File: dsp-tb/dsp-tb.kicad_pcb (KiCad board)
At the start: 2 copper layers, 24 parts, among them J10 USB_C_Receptacle_USB2.0, J2 Conn_ARM_SWD_TagConnect_TC2030, J9 104031-0811, U1 STM32H723ZGTx, U10 FSUSB42UMX, U11 CS4270-CZZ, U12 TLV9301xDBV, U13 TLV9301xDBV, U14 TLV9301xDBV, U15 TLV9301xDBV, U2 TLV76733QWDRBxQ1, U4 NCP718xSN500, U5 D3V3XA4B10LP, U6 IS42S16800F-7BL-TR, U7 IS25LP080D-JNLE, U8 USB3318C-CP-TR, U9 ASDMB-xxxMHz

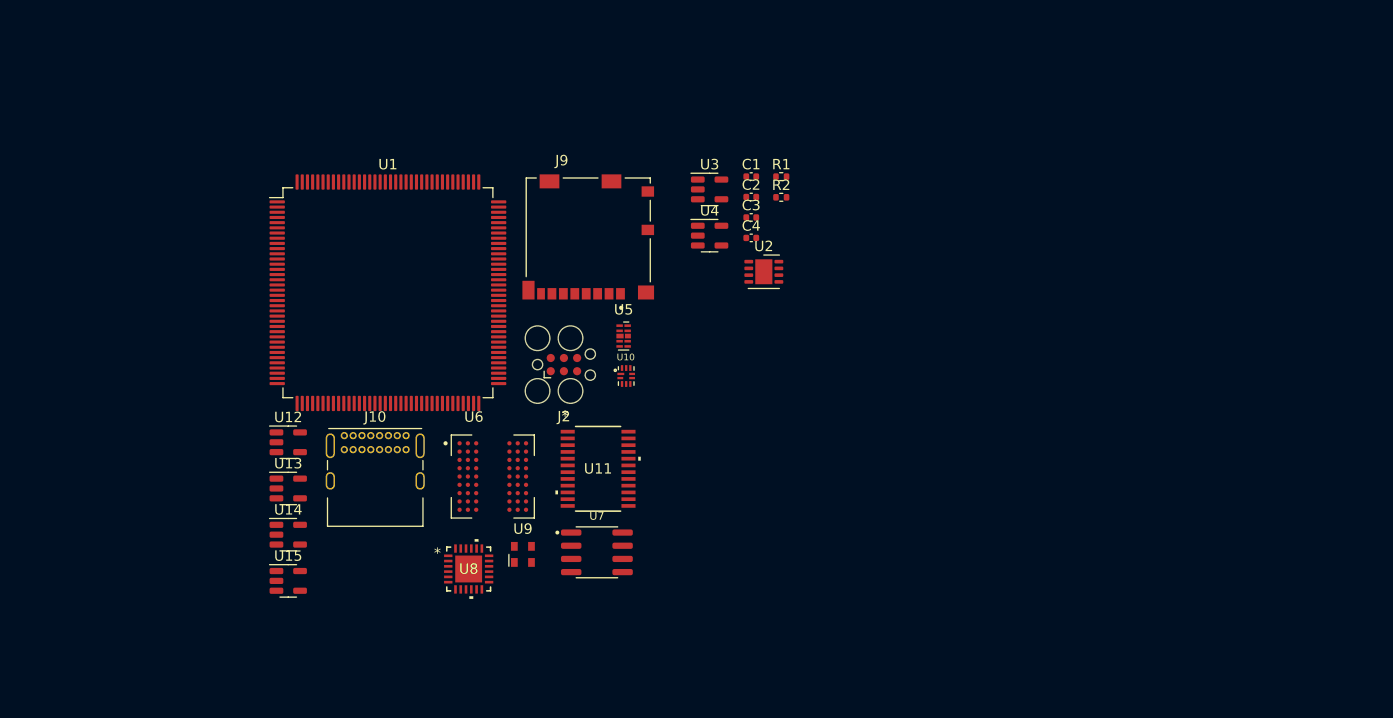
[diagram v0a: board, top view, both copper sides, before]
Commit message: dsp-tb: start to include external components for mcu
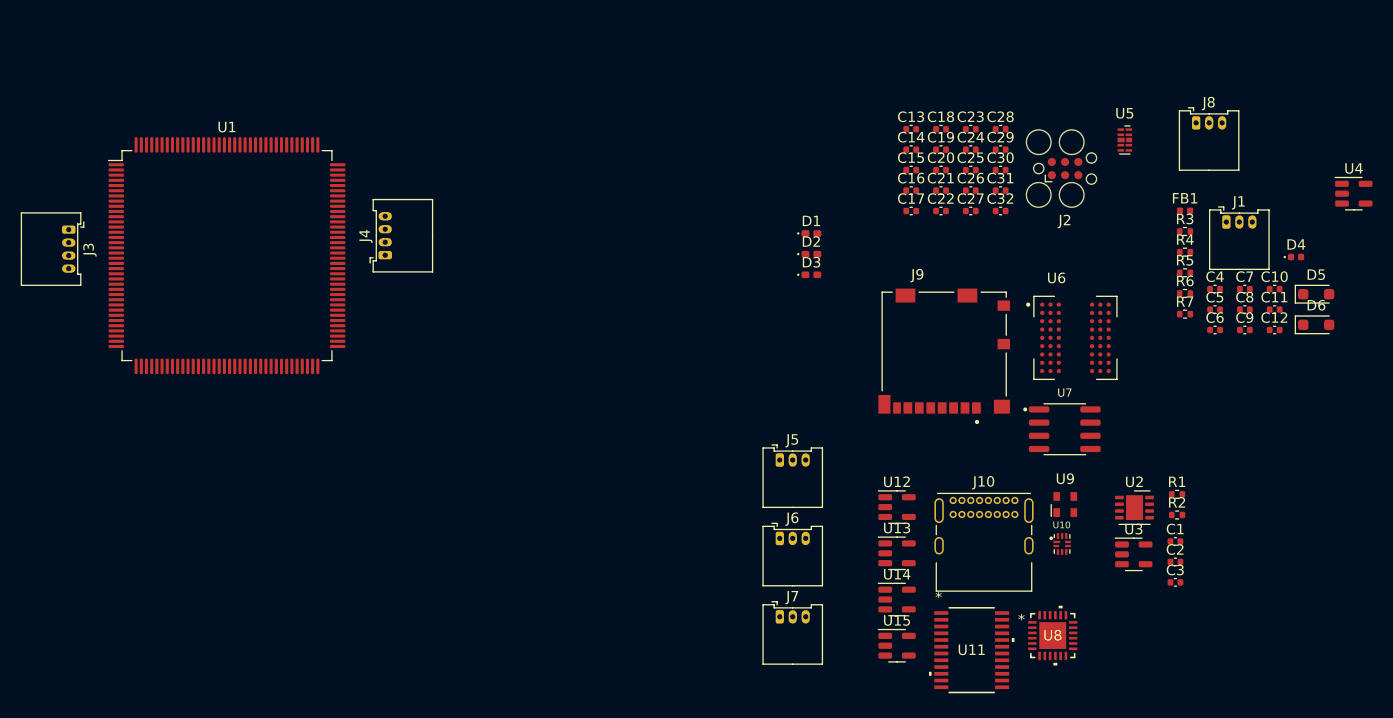
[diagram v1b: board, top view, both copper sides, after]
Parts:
- added C10: 47u, Capacitor_SMD:C_0402_1005Metric, F.Cu at (233.0, 87.0)
- added C11: 47u, Capacitor_SMD:C_0402_1005Metric, F.Cu at (233.0, 89.0)
- added C12: 47u, Capacitor_SMD:C_0402_1005Metric, F.Cu at (233.0, 91.0)
- added C13: 2u2, Capacitor_SMD:C_0402_1005Metric, F.Cu at (198.0, 71.6)
- added C14: 2u2, Capacitor_SMD:C_0402_1005Metric, F.Cu at (198.0, 73.6)
- added C15: 100n, Capacitor_SMD:C_0402_1005Metric, F.Cu at (198.0, 75.6)
- added C16: 100n, Capacitor_SMD:C_0402_1005Metric, F.Cu at (198.0, 77.6)
- added C17: 100n, Capacitor_SMD:C_0402_1005Metric, F.Cu at (198.0, 79.5)
- added C18: 100n, Capacitor_SMD:C_0402_1005Metric, F.Cu at (200.8, 71.6)
- added C19: 100n, Capacitor_SMD:C_0402_1005Metric, F.Cu at (200.8, 73.6)
- added C20: 100n, Capacitor_SMD:C_0402_1005Metric, F.Cu at (200.8, 75.6)
- added C21: 100n, Capacitor_SMD:C_0402_1005Metric, F.Cu at (200.8, 77.6)
- added C22: 100n, Capacitor_SMD:C_0402_1005Metric, F.Cu at (200.8, 79.5)
- added C23: 100n, Capacitor_SMD:C_0402_1005Metric, F.Cu at (203.7, 71.6)
- added C24: 100n, Capacitor_SMD:C_0402_1005Metric, F.Cu at (203.7, 73.6)
- added C25: 100n, Capacitor_SMD:C_0402_1005Metric, F.Cu at (203.7, 75.6)
- added C26: 100n, Capacitor_SMD:C_0402_1005Metric, F.Cu at (203.7, 77.6)
- added C27: 100n, Capacitor_SMD:C_0402_1005Metric, F.Cu at (203.7, 79.5)
- added C28: 100n, Capacitor_SMD:C_0402_1005Metric, F.Cu at (206.6, 71.6)
- added C29: 100n, Capacitor_SMD:C_0402_1005Metric, F.Cu at (206.6, 73.6)
- added C30: 100n, Capacitor_SMD:C_0402_1005Metric, F.Cu at (206.6, 75.6)
- added C31: 100n, Capacitor_SMD:C_0402_1005Metric, F.Cu at (206.6, 77.6)
- added C32: 2u2, Capacitor_SMD:C_0402_1005Metric, F.Cu at (206.6, 79.5)
- added C5: 2u2, Capacitor_SMD:C_0402_1005Metric, F.Cu at (227.2, 89.0)
- added C6: 2u2, Capacitor_SMD:C_0402_1005Metric, F.Cu at (227.2, 91.0)
- added C7: 2u2, Capacitor_SMD:C_0402_1005Metric, F.Cu at (230.1, 87.0)
- added C8: 2u2, Capacitor_SMD:C_0402_1005Metric, F.Cu at (230.1, 89.0)
- added C9: 47u, Capacitor_SMD:C_0402_1005Metric, F.Cu at (230.1, 91.0)
- added D1: RED, LED_SMD:LED_0402_1005Metric_Pad0.77x0.64mm_HandSolder, F.Cu at (188.4, 81.7)
- added D2: YLW, LED_SMD:LED_0402_1005Metric_Pad0.77x0.64mm_HandSolder, F.Cu at (188.4, 83.7)
- added D3: BLU, LED_SMD:LED_0402_1005Metric_Pad0.77x0.64mm_HandSolder, F.Cu at (188.4, 85.7)
- added D4: CG0402MLU-12G, Diode_SMD:D_0402_1005Metric, F.Cu at (235.0, 84.0)
- added D5: BAT165A, Diode_SMD:D_SOD-323_HandSoldering, F.Cu at (237.0, 87.5)
- added D6: BAT165A, Diode_SMD:D_SOD-323_HandSoldering, F.Cu at (237.0, 90.5)
- added FB1: FerriteBead, Inductor_SMD:L_0402_1005Metric, F.Cu at (224.3, 79.5)
- added J1: Conn_01x03, Connector_Molex:Molex_PicoBlade_53048-0310_1x03_P1.25mm_Horizontal, F.Cu at (228.3, 80.6)
- added J3: Conn_01x04, Connector_Molex:Molex_PicoBlade_53048-0410_1x04_P1.25mm_Horizontal, F.Cu at (116.8, 81.3)
- added J4: Conn_01x04, Connector_Molex:Molex_PicoBlade_53048-0410_1x04_P1.25mm_Horizontal, F.Cu at (147.3, 83.8)
- added J5: Conn_01x03, Connector_Molex:Molex_PicoBlade_53048-0310_1x03_P1.25mm_Horizontal, F.Cu at (185.3, 103.5)
- added J6: Conn_01x03, Connector_Molex:Molex_PicoBlade_53048-0310_1x03_P1.25mm_Horizontal, F.Cu at (185.3, 111.1)
- added J7: Conn_01x03, Connector_Molex:Molex_PicoBlade_53048-0310_1x03_P1.25mm_Horizontal, F.Cu at (185.3, 118.6)
- added J8: Conn_01x03, Connector_Molex:Molex_PicoBlade_53048-0310_1x03_P1.25mm_Horizontal, F.Cu at (225.4, 71.0)
- added R3: 47k, Resistor_SMD:R_0402_1005Metric, F.Cu at (224.3, 81.5)
- added R4: 15k, Resistor_SMD:R_0402_1005Metric, F.Cu at (224.3, 83.5)
- added R5: 47k, Resistor_SMD:R_0402_1005Metric, F.Cu at (224.3, 85.5)
- added R6: 91k, Resistor_SMD:R_0402_1005Metric, F.Cu at (224.3, 87.5)
- added R7: 10, Resistor_SMD:R_0402_1005Metric, F.Cu at (224.3, 89.5)
- U3: value ~ -> NCP718BSNADJT1G
- U4: value NCP718xSN500 -> NCP718BSNADJT1G
- moved U4 62.2 mm to (240.6, 77.9)
- moved U12 59.0 mm to (196.6, 108.0)
- moved U14 59.0 mm to (196.6, 116.9)
- moved U15 59.0 mm to (196.6, 121.4)
- moved U13 59.0 mm to (196.6, 112.5)
- moved J10 59.0 mm to (202.0, 107.4)
- moved U6 57.7 mm to (213.8, 91.7)
- moved U8 56.6 mm to (211.6, 120.4)
- moved C3 53.9 mm to (223.4, 115.3)
- moved U3 53.9 mm to (219.4, 112.6)
- moved C1 53.9 mm to (223.4, 111.3)
- moved C2 53.9 mm to (223.4, 113.3)
- moved U9 52.5 mm to (212.8, 107.8)
- moved J2 51.8 mm to (212.8, 75.4)
- moved U5 51.8 mm to (218.5, 72.7)
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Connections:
- C1 pad 1: Net-(U2-EN) -> Net-(D6-K)
- C2 pad 1: unconnected-(C2-Pad1) -> +3V3
- C2 pad 2: unconnected-(C2-Pad2) -> GND
- C3 pad 1: Net-(U2-OUT) -> Net-(D6-K)
- C4 pad 1: Net-(U3-EN) -> +5V
- C4 pad 2: unconnected-(C4-Pad2) -> GND
- R1 pad 1: Net-(U2-OUT) -> +3V3
- U1 pad 106: unconnected-(U1-VCAP-Pad106) -> Net-(C14-Pad1)
- U1 pad 71: unconnected-(U1-VCAP-Pad71) -> Net-(C13-Pad1)
- U2 pad 1: Net-(U2-OUT) -> +3V3
- U2 pad 5: Net-(U2-EN) -> Net-(D6-K)
- U2 pad 8: Net-(U2-EN) -> Net-(D6-K)
- U3 pad 1: Net-(U3-EN) -> Net-(D6-K)
- U3 pad 2: unconnected-(U3-GND-Pad2) -> GND
- U3 pad 3: Net-(U3-EN) -> Net-(D6-K)
- U3 pad 4: unconnected-(U3-ADJ-Pad4) -> Net-(U3-ADJ)
- U3 pad 5: unconnected-(U3-OUT-Pad5) -> +5V
- U4 pad 1: unconnected-(U4-IN-Pad1) -> +3V3
- U4 pad 2: unconnected-(U4-GND-Pad2) -> GND
- U4 pad 3: unconnected-(U4-EN-Pad3) -> +3V3
- U4 pad 4: unconnected-(U4-NC-Pad4) -> Net-(U4-ADJ)
- U4 pad 5: unconnected-(U4-OUT-Pad5) -> +1V8

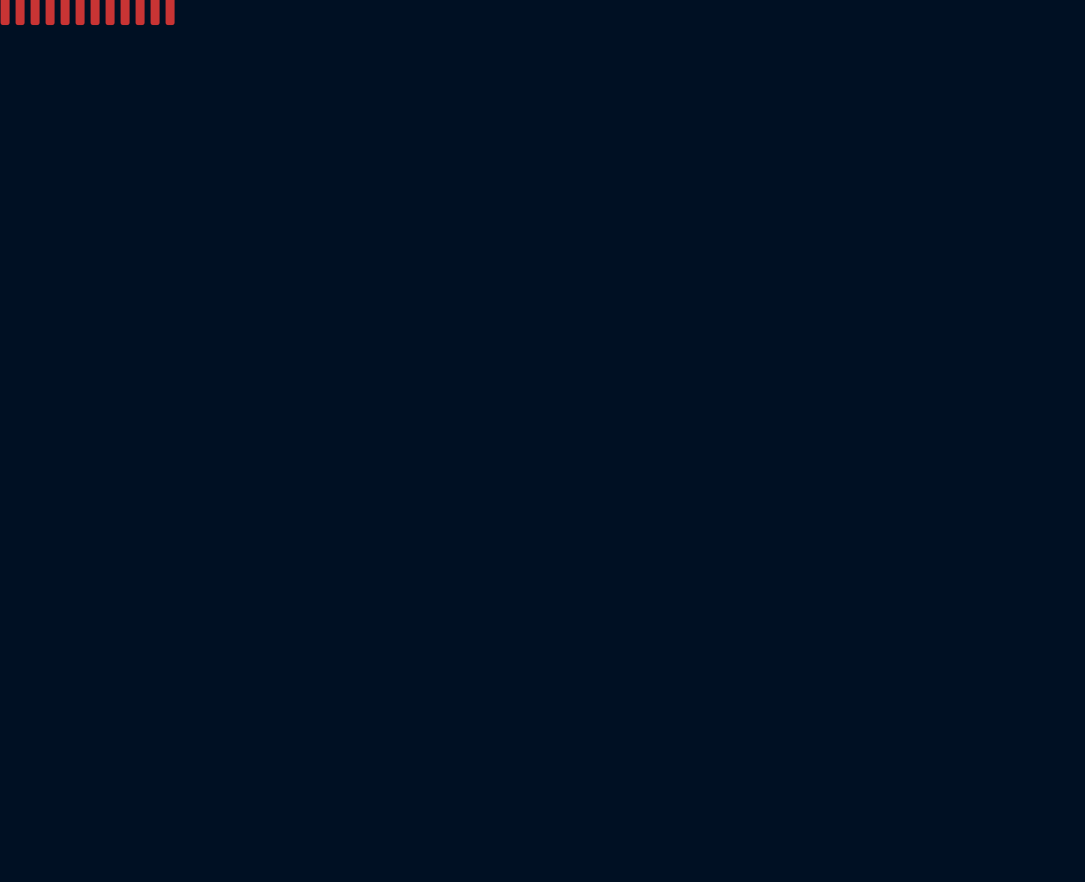
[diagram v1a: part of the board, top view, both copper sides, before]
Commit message: dsp: boot0 and reset switches
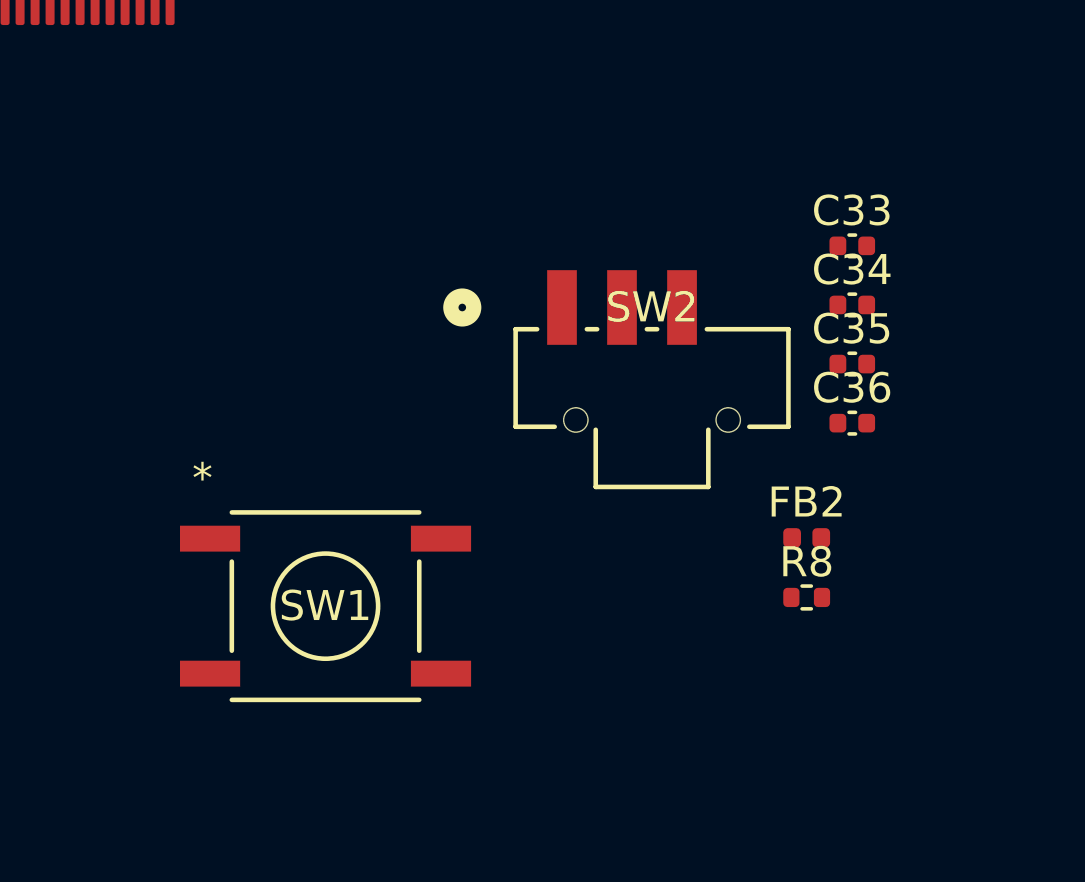
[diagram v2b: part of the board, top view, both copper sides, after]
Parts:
- added C33: 100n, Capacitor_SMD:C_0402_1005Metric, F.Cu at (163.6, 102.6)
- added C34: 100n, Capacitor_SMD:C_0402_1005Metric, F.Cu at (163.6, 104.5)
- added C35: 100n, Capacitor_SMD:C_0402_1005Metric, F.Cu at (163.6, 106.5)
- added C36: 100n, Capacitor_SMD:C_0402_1005Metric, F.Cu at (163.6, 108.5)
- added FB2: 120R@100Mhz, Inductor_SMD:L_0402_1005Metric, F.Cu at (162.1, 112.3)
- added R8: 10k, Resistor_SMD:R_0402_1005Metric, F.Cu at (162.1, 114.3)
- added SW1: SW_MEC_5E, footprints:PTS645SL43SMTR92LFS_CNK, F.Cu at (146.0, 114.6)
- added SW2: SW_SPDT, footprints:CSS-1210TB_NDC, F.Cu at (156.9, 107.0)
- FB1: value FerriteBead -> 120R@100MHz
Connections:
- C15 pad 1: unconnected-(C15-Pad1) -> +3V3
- C15 pad 2: unconnected-(C15-Pad2) -> GND
- C16 pad 1: unconnected-(C16-Pad1) -> +3V3
- C16 pad 2: unconnected-(C16-Pad2) -> GND
- C17 pad 1: unconnected-(C17-Pad1) -> +3V3
- C17 pad 2: unconnected-(C17-Pad2) -> GND
- C18 pad 1: unconnected-(C18-Pad1) -> +3V3
- C18 pad 2: unconnected-(C18-Pad2) -> GND
- C19 pad 1: unconnected-(C19-Pad1) -> +3V3
- C19 pad 2: unconnected-(C19-Pad2) -> GND
- C20 pad 1: unconnected-(C20-Pad1) -> +3V3
- C20 pad 2: unconnected-(C20-Pad2) -> GND
- C21 pad 1: unconnected-(C21-Pad1) -> +3V3
- C21 pad 2: unconnected-(C21-Pad2) -> GND
- C22 pad 1: unconnected-(C22-Pad1) -> +3V3
- C22 pad 2: unconnected-(C22-Pad2) -> GND
- C23 pad 1: unconnected-(C23-Pad1) -> +3V3
- C23 pad 2: unconnected-(C23-Pad2) -> GND
- C24 pad 1: unconnected-(C24-Pad1) -> +3V3
- C24 pad 2: unconnected-(C24-Pad2) -> GND
- C25 pad 1: unconnected-(C25-Pad1) -> +3V3
- C25 pad 2: unconnected-(C25-Pad2) -> GND
- C26 pad 1: unconnected-(C26-Pad1) -> +3V3
- C26 pad 2: unconnected-(C26-Pad2) -> GND
- C27 pad 1: unconnected-(C27-Pad1) -> +3V3
- C27 pad 2: unconnected-(C27-Pad2) -> GND
- C28 pad 1: unconnected-(C28-Pad1) -> +3V3
- C28 pad 2: unconnected-(C28-Pad2) -> GND
- C29 pad 1: unconnected-(C29-Pad1) -> +3V3
- C29 pad 2: unconnected-(C29-Pad2) -> GND
- C30 pad 1: unconnected-(C30-Pad1) -> +3V3
- C30 pad 2: unconnected-(C30-Pad2) -> GND
- C31 pad 1: unconnected-(C31-Pad1) -> +3V3
- C31 pad 2: unconnected-(C31-Pad2) -> GND
- C32 pad 1: unconnected-(C32-Pad1) -> +3V3
- C32 pad 2: unconnected-(C32-Pad2) -> GND
- U1 pad 108: unconnected-(U1-VDD-Pad108) -> +3V3
- U1 pad 121: unconnected-(U1-VDD-Pad121) -> +3V3
- U1 pad 131: unconnected-(U1-VDD-Pad131) -> +3V3
- U1 pad 138: unconnected-(U1-BOOT0-Pad138) -> Net-(U1-BOOT0)
- U1 pad 144: unconnected-(U1-VDD-Pad144) -> +3V3
- U1 pad 17: unconnected-(U1-VDD-Pad17) -> +3V3
- U1 pad 25: unconnected-(U1-NRST-Pad25) -> Net-(SW1-A)
- U1 pad 30: unconnected-(U1-VDD-Pad30) -> +3V3
- U1 pad 32: unconnected-(U1-VREF+-Pad32) -> +3.3VA
- U1 pad 33: unconnected-(U1-VDDA-Pad33) -> +3.3VA
- U1 pad 39: unconnected-(U1-VDD-Pad39) -> +3V3
- U1 pad 52: unconnected-(U1-VDD-Pad52) -> +3V3
- U1 pad 6: unconnected-(U1-VBAT-Pad6) -> +3V3
- U1 pad 62: unconnected-(U1-VDD-Pad62) -> +3V3
- U1 pad 72: unconnected-(U1-VDD-Pad72) -> +3V3
- U1 pad 84: unconnected-(U1-VDD-Pad84) -> +3V3
- U1 pad 95: unconnected-(U1-VDD33USB-Pad95) -> +3V3
